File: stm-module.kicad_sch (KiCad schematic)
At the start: 36 parts, among them J1 Conn_01x05_Pin, J2 connectorL, J3 connectorR, J4 power, J5 USB_C_Receptacle_USB2.0_16P, SW1 Reset, U1 STM32G474RETx, U2 TPS7A20xxxDBV, Y1 Crystal

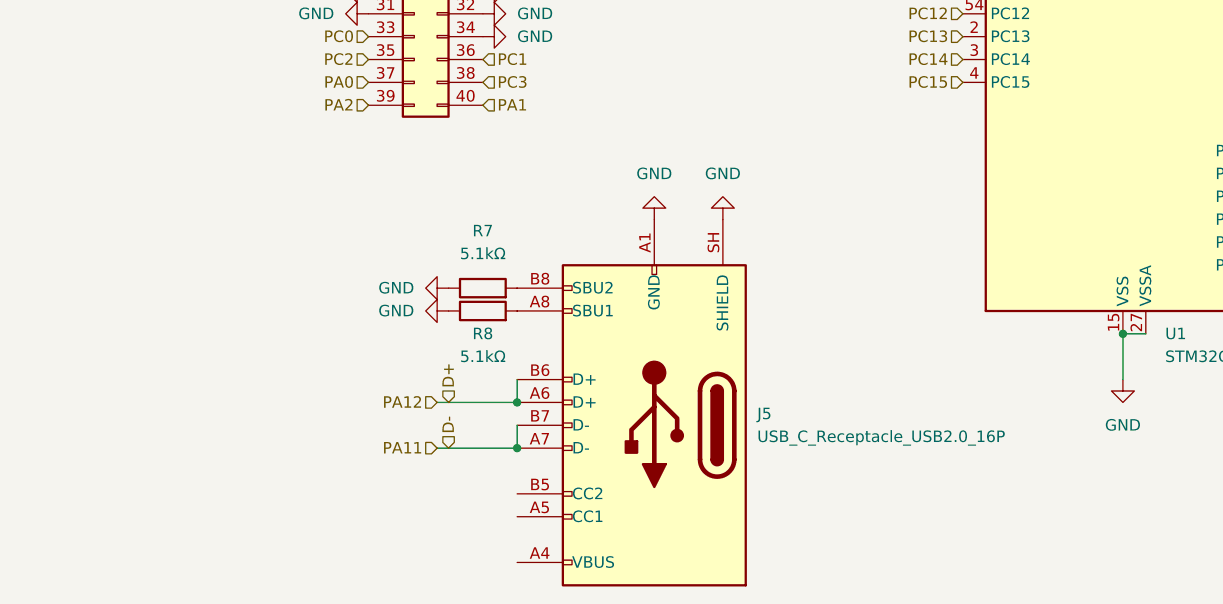
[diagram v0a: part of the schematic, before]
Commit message: change usbc symbol
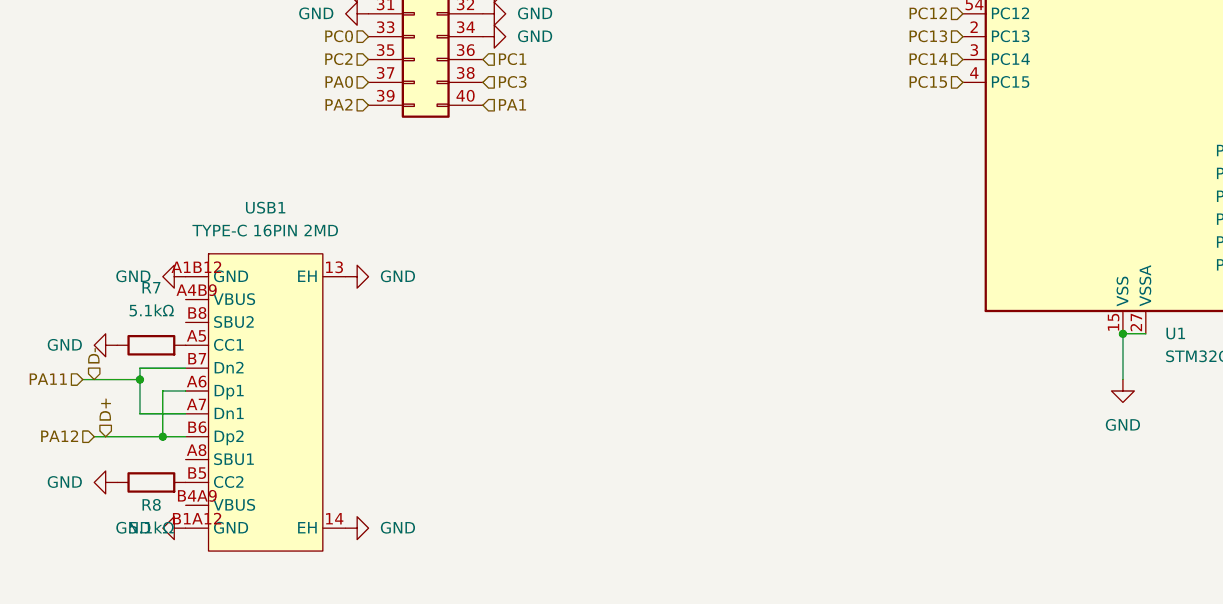
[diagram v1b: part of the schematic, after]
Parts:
- removed J5: USB_C_Receptacle_USB2.0_16P, Connector_USB:USB_C_Receptacle_HRO_TYPE-C-31-M-12, symbol Connector:USB_C_Receptacle_USB2.0_16P
- added USB1: TYPE-C 16PIN 2MD, EasyEDA:USB-C-SMD_TYPE-C-16PIN-2MD-073, symbol EasyEDA:TYPE-C16PIN2MD
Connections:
- net D+: now also USB1.A6 (Dp1), USB1.B6 (Dp2)
- net D-: now also USB1.A7 (Dn1), USB1.B7 (Dn2)
- net GND: now also USB1.13 (EH), USB1.14 (EH), USB1.A1B12 (GND), USB1.B1A12 (GND)
- net at R8.2: now also USB1.B5 (CC2)
- net at R7.2: now also USB1.A5 (CC1)

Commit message: pcb updates and gitignore update
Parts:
- C13, C4, C5, C6, C7, C8: LCSC Part # (none) -> C1856507
- C14, C2, C9: LCSC Part # (none) -> C107367
- C15: LCSC Part # (none) -> C17024
- R2: LCSC Part # (none) -> C17414
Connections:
- net +3.3V: now also J3.17 (Pin_17)
- net GND: no longer J3.17 (Pin_17)
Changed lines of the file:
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@@
 			)
 		)
-		(property "LCSC Part #" ""
+		(property "LCSC Part #" "C17024"
 			(at 50.8 43.18 0)
 			(hide yes)
@@
 			)
 		)
-		(property "LCSC Part #" ""
+		(property "LCSC Part #" "C107367"
 			(at 121.92 57.15 90)
 			(hide yes)
@@
 	)
 	(symbol
-		(lib_id "power:GND")
-		(at 217.17 88.9 270)
-		(unit 1)
-		(body_style 1)
-		(exclude_from_sim no)
-		(in_bom yes)
-		(on_board yes)
-		(in_pos_files yes)
-		(dnp no)
-		(fields_autoplaced yes)
-		(property "Reference" "#PWR060"
-			(at 210.82 88.9 0)
-			(hide yes)
-			(show_name no)
-			(do_not_autoplace no)
-			(effects
-				(font
-					(size 1.27 1.27)
-				)
-			)
-		)
-		(property "Value" "GND"
-			(at 213.36 88.8999 90)
-			(show_name no)
-			(do_not_autoplace no)
-			(effects
-				(font
-					(size 1.27 1.27)
-				)
-				(justify right)
-			)
-		)
-		(property "Footprint" ""
-			(at 217.17 88.9 0)
-			(hide yes)
-			(show_name no)
-			(do_not_autoplace no)
-			(effects
-				(font
-					(size 1.27 1.27)
-				)
-			)
-		)
-		(property "Datasheet" ""
-			(at 217.17 88.9 0)
-			(hide yes)
-			(show_name no)
-			(do_not_autoplace no)
-			(effects
-				(font
-					(size 1.27 1.27)
-				)
-			)
-		)
-		(property "Description" "Power symbol creates a global label with name \"GND\" , ground"
-			(at 217.17 88.9 0)
-			(hide yes)
-			(show_name no)
-			(do_not_autoplace no)
-			(effects
-				(font
-					(size 1.27 1.27)
-				)
-			)
-		)
-		(pin "1"
-		)
-		(instances
-			(project "stm-module"
-				(path "/62d736bd-c9d5-4ff1-9607-8a775f0da7bc"
-					(reference "#PWR060")
-					(unit 1)
-				)
-			)
-		)
-	)
-	(symbol
 		(lib_id "Device:C")
 		(at 143.51 50.8 0)
@@
 			)
 		)
-		(property "LCSC Part #" ""
+		(property "LCSC Part #" "C1856507"
 			(at 143.51 50.8 0)
 			(hide yes)
@@
 			)
 		)
-		(property "LCSC Part #" ""
+		(property "LCSC Part #" "C107367"
 			(at 161.29 62.23 90)
 			(hide yes)
@@
 			)
 		)
-		(property "LCSC Part #" ""
+		(property "LCSC Part #" "C1856507"
 			(at 121.92 66.04 90)
 			(hide yes)
@@
 			)
 		)
-		(property "LCSC Part #" ""
+		(property "LCSC Part #" "C1856507"
 			(at 153.67 50.8 0)
 			(hide yes)
@@
 	)
 	(symbol
+		(lib_id "power:+3.3V")
+		(at 217.17 88.9 90)
+		(unit 1)
+		(body_style 1)
+		(exclude_from_sim no)
+		(in_bom yes)
+		(on_board yes)
+		(in_pos_files yes)
+		(dnp no)
+		(fields_autoplaced yes)
+		(property "Reference" "#PWR017"
+			(at 220.98 88.9 0)
+			(hide yes)
+			(show_name no)
+			(do_not_autoplace no)
+			(effects
+				(font
+					(size 1.27 1.27)
+				)
+			)
+		)
+		(property "Value" "+3.3V"
+			(at 213.36 88.8999 90)
+			(show_name no)
+			(do_not_autoplace no)
+			(effects
+				(font
+					(size 1.27 1.27)
+				)
+				(justify left)
+			)
+		)
+		(property "Footprint" ""
+			(at 217.17 88.9 0)
+			(hide yes)
+			(show_name no)
+			(do_not_autoplace no)
+			(effects
+				(font
+					(size 1.27 1.27)
+				)
+			)
+		)
+		(property "Datasheet" ""
+			(at 217.17 88.9 0)
+			(hide yes)
+			(show_name no)
+			(do_not_autoplace no)
+			(effects
+				(font
+					(size 1.27 1.27)
+				)
+			)
+		)
+		(property "Description" "Power symbol creates a global label with name \"+3.3V\""
+			(at 217.17 88.9 0)
+			(hide yes)
+			(show_name no)
+			(do_not_autoplace no)
+			(effects
+				(font
+					(size 1.27 1.27)
+				)
+			)
+		)
+		(pin "1"
+		)
+		(instances
+			(project "stm-module"
+				(path "/62d736bd-c9d5-4ff1-9607-8a775f0da7bc"
+					(reference "#PWR017")
+					(unit 1)
+				)
+			)
+		)
+	)
+	(symbol
 		(lib_id "Switch:SW_Push")
 		(at 113.03 83.82 0)
@@
 			)
 		)
-		(property "LCSC Part #" ""
+		(property "LCSC Part #" "C1856507"
 			(at 151.13 50.8 0)
 			(hide yes)
@@
 			)
 		)
-		(property "LCSC Part #" ""
+		(property "LCSC Part #" "C17414"
 			(at 184.15 134.62 90)
 			(hide yes)
@@
 			)
 		)
-		(property "LCSC Part #" ""
+		(property "LCSC Part #" "C107367"
 			(at 57.15 43.18 0)
 			(hide yes)
@@
 			)
 		)
-		(property "LCSC Part #" ""
+		(property "LCSC Part #" "C1856507"
 			(at 146.05 50.8 0)
 			(hide yes)
@@
 			)
 		)
-		(property "LCSC Part #" ""
+		(property "LCSC Part #" "C1856507"
 			(at 148.59 50.8 0)
 			(hide yes)
